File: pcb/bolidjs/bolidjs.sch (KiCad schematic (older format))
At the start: 62 parts, among them J1 Vext, J11 rearL+, J12 rearL-, J13 rearR+, J14 rearR-, J17 frontL, J18 f1L, J19 f2L, J20 frontR, J21 f1R, J22 f2R, J23 frontBar, J24 VCC, J25 D14, J26 D29, J27 D15, J28 D31, J3 FL, J34 BM, J35 BM, J36 VDD, J4 FR, J5 F, J6 END1, J7 END1, J8 END2, J9 END2, M1 Stepper, U1 MDB42Q_brkout, U2 LB1930MC-AH, U3 LB1930MC-AH, U4 LB1930MC-AH, U5 LB1930MC-AH

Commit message: adding pdf for schematic and layout
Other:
- note added: "* duplicate pads for different motor sizes"
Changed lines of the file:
@@
 Wire Bus Line
 	4100 2000 4100 3600
+Text Notes 10950 4750 1    50   ~ 0
+* duplicate pads for different motor sizes
 $EndSCHEMATC

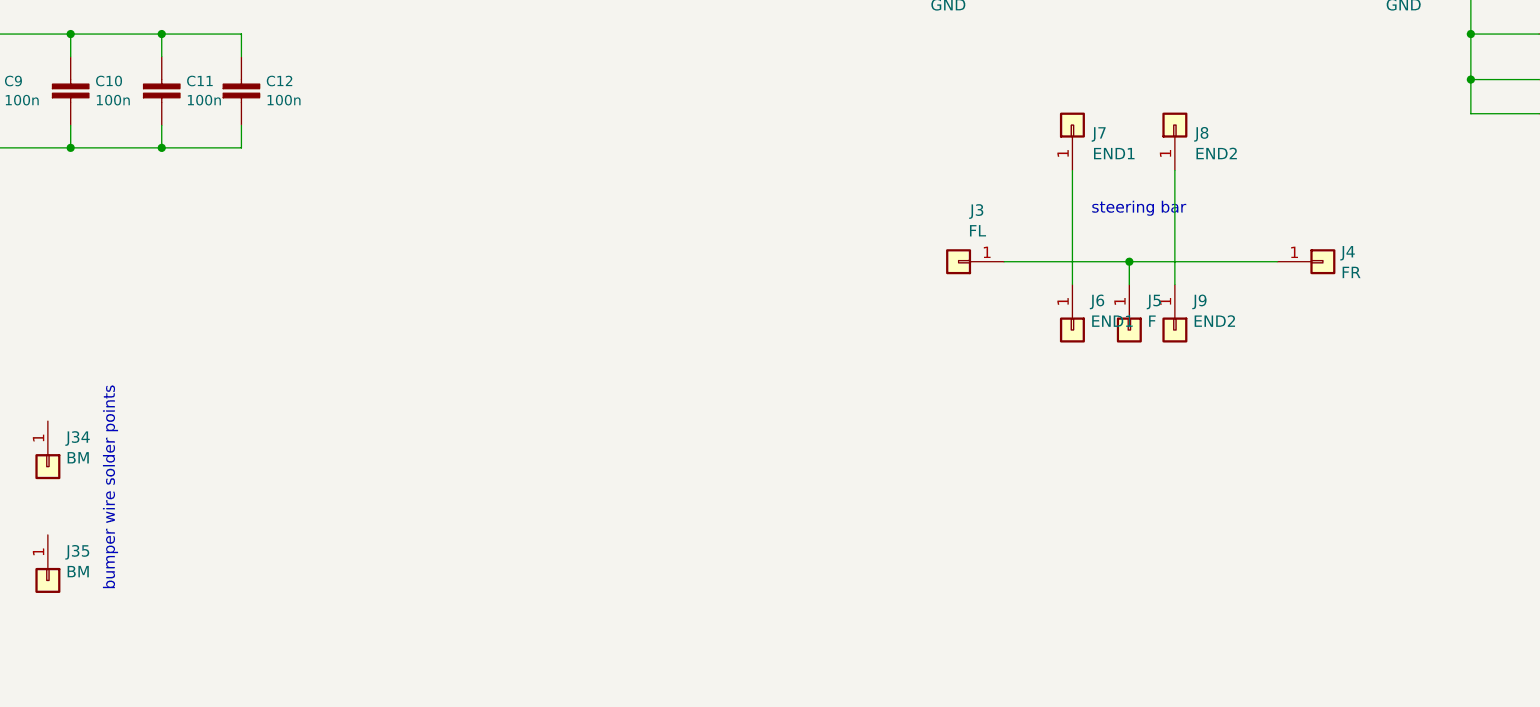
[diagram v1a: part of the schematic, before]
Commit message: added steering option and wheel pads
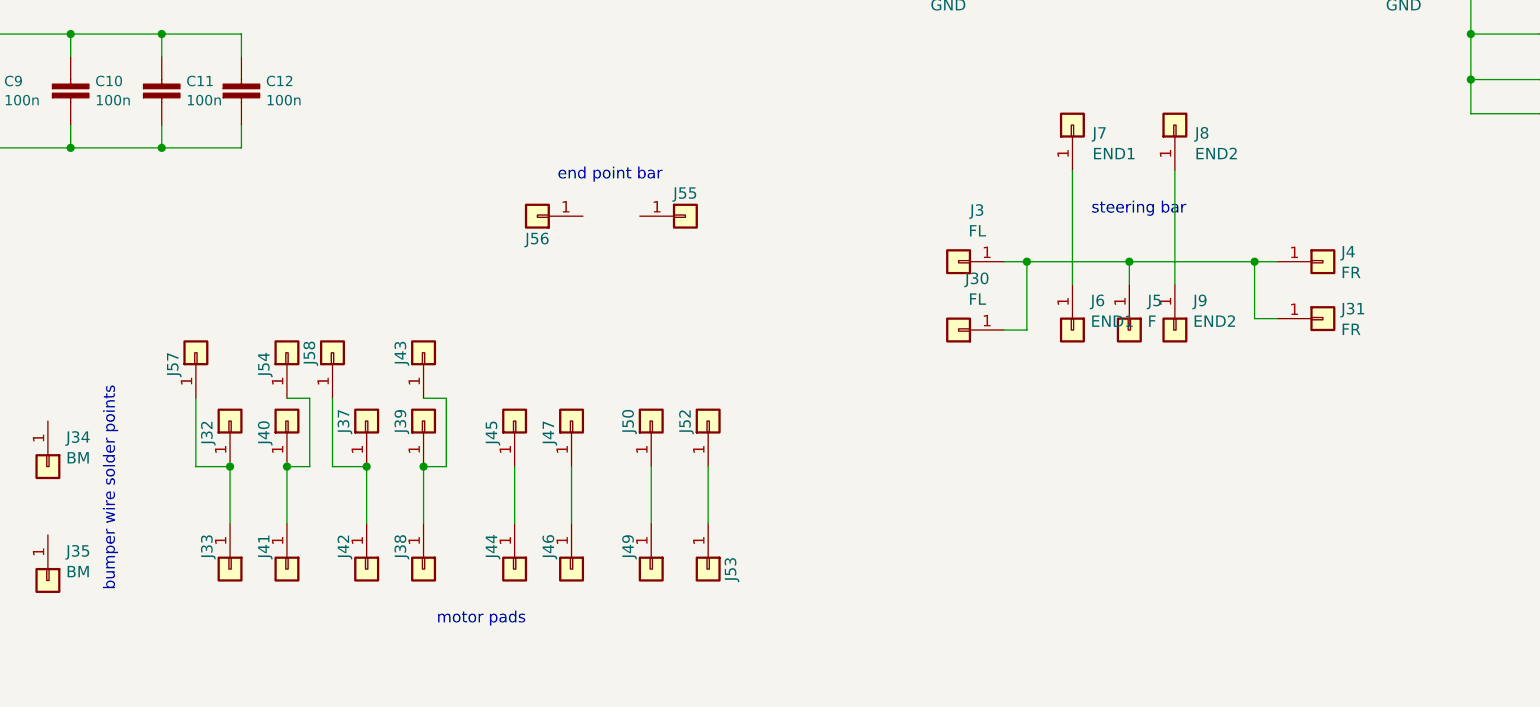
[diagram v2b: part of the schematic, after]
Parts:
- added J30, J32, J33, J37, J38, J39, J40, J41, J42, J43, J44, J45, J46, J47, J49, J50, J52, J53, J54, J55, J56, J57, J58: FL, Connector_PinHeader_2.54mm:PinHeader_1x01_P2.54mm_Vertical, symbol Connector_Generic:Conn_01x01
- added J31: FR, Connector_PinHeader_2.54mm:PinHeader_1x01_P2.54mm_Vertical, symbol Connector_Generic:Conn_01x01
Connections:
- net at J3.1 (Pin_1), J4.1 (Pin_1), J5.1 (Pin_1): now also J30.1 (Pin_1), J31.1 (Pin_1)
- new net: J32.1 (Pin_1), J33.1 (Pin_1), J57.1 (Pin_1)
- new net: J40.1 (Pin_1), J41.1 (Pin_1), J54.1 (Pin_1)
- new net: J37.1 (Pin_1), J42.1 (Pin_1), J58.1 (Pin_1)
- new net: J38.1 (Pin_1), J39.1 (Pin_1), J43.1 (Pin_1)
- new net: J44.1 (Pin_1), J45.1 (Pin_1)
- new net: J46.1 (Pin_1), J47.1 (Pin_1)
- new net: J49.1 (Pin_1), J50.1 (Pin_1)
- new net: J52.1 (Pin_1), J53.1 (Pin_1)
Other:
- note added: "end point bar"
- note added: "motor pads"

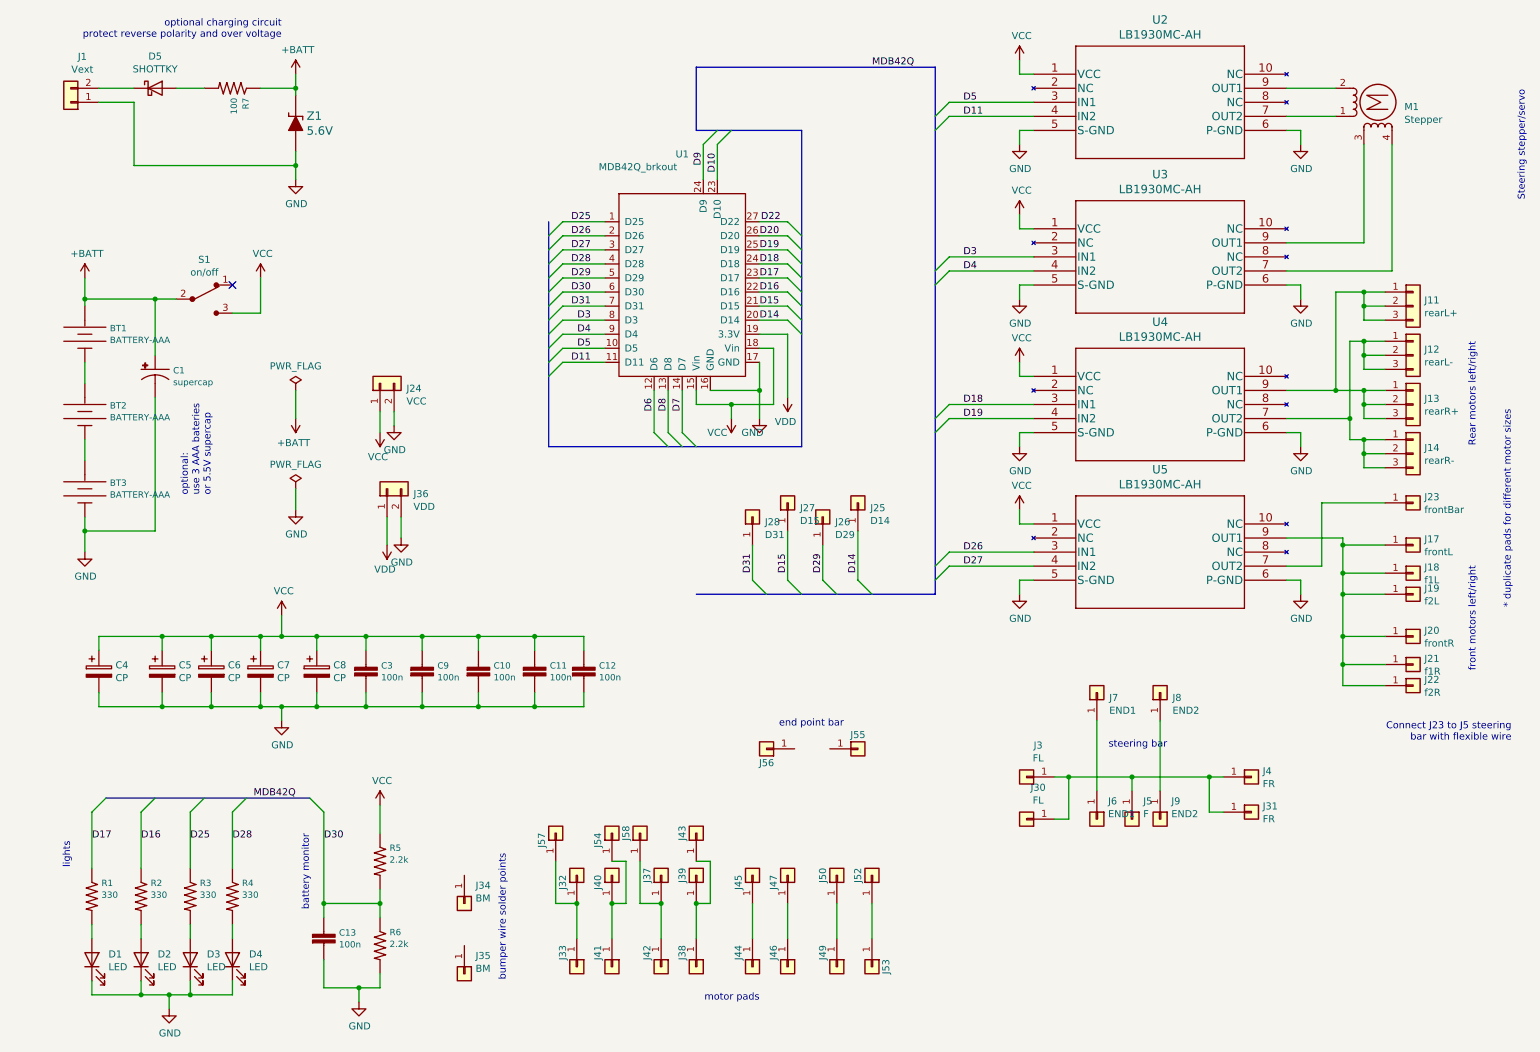
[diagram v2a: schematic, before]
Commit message: removed options for motor sizes
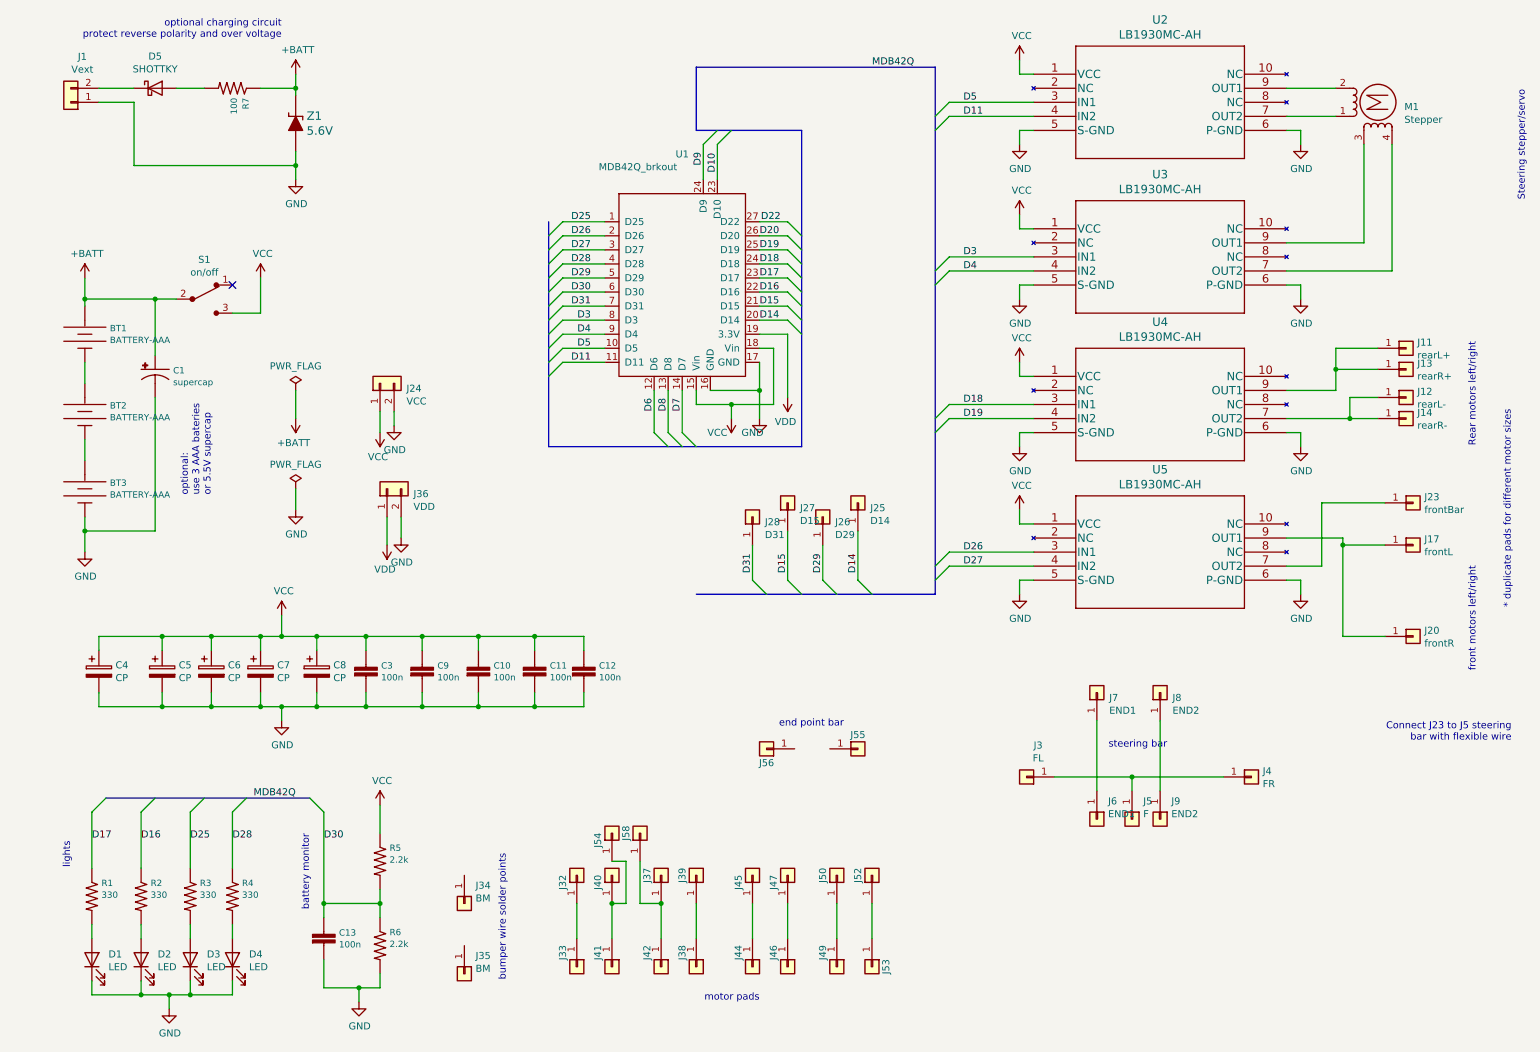
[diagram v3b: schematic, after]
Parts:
- removed J11: rearL+, Connector_PinHeader_2.54mm:PinHeader_1x03_P2.54mm_Vertical, symbol Connector_Generic:Conn_01x03
- removed J12: rearL-, Connector_PinHeader_2.54mm:PinHeader_1x03_P2.54mm_Vertical, symbol Connector_Generic:Conn_01x03
- removed J13: rearR+, Connector_PinHeader_2.54mm:PinHeader_1x03_P2.54mm_Vertical, symbol Connector_Generic:Conn_01x03
- removed J14: rearR-, Connector_PinHeader_2.54mm:PinHeader_1x03_P2.54mm_Vertical, symbol Connector_Generic:Conn_01x03
- removed J18: f1L, Connector_PinHeader_2.54mm:PinHeader_1x01_P2.54mm_Vertical, symbol Connector_Generic:Conn_01x01
- removed J19: f2L, Connector_PinHeader_2.54mm:PinHeader_1x01_P2.54mm_Vertical, symbol Connector_Generic:Conn_01x01
- removed J21: f1R, Connector_PinHeader_2.54mm:PinHeader_1x01_P2.54mm_Vertical, symbol Connector_Generic:Conn_01x01
- removed J22: f2R, Connector_PinHeader_2.54mm:PinHeader_1x01_P2.54mm_Vertical, symbol Connector_Generic:Conn_01x01
- removed J30, J43, J57: FL, Connector_PinHeader_2.54mm:PinHeader_1x01_P2.54mm_Vertical, symbol Connector_Generic:Conn_01x01
- removed J31: FR, Connector_PinHeader_2.54mm:PinHeader_1x01_P2.54mm_Vertical, symbol Connector_Generic:Conn_01x01
- added J11: rearL+, Connector_PinHeader_2.54mm:PinHeader_1x01_P2.54mm_Vertical, symbol Connector_Generic:Conn_01x01
- added J12: rearL-, Connector_PinHeader_2.54mm:PinHeader_1x01_P2.54mm_Vertical, symbol Connector_Generic:Conn_01x01
- added J13: rearR+, Connector_PinHeader_2.54mm:PinHeader_1x01_P2.54mm_Vertical, symbol Connector_Generic:Conn_01x01
- added J14: rearR-, Connector_PinHeader_2.54mm:PinHeader_1x01_P2.54mm_Vertical, symbol Connector_Generic:Conn_01x01
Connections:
- net at U4.7 (OUT2): now also J12.1 (Pin_1), J14.1 (Pin_1)
- net at U4.9 (OUT1): now also J11.1 (Pin_1), J13.1 (Pin_1)
